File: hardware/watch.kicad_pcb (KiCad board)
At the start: 4 copper layers, 39.1 x 36.1 mm, 77 parts, among them J1 DX07S016JA1R1500, J601 SWD, Q1 DMN6140L, Q401 DMP2110UW-7, Q701 DMP2110UW-7, SW601 SW_Push, SW602 SW_Push, U12 TCPP01-M12, U201 KCSA02-105, U202 STP08DP05, U203 KCSA02-105, U204 STP08DP05, U205 KCSA02-105, U206 STP08DP05, U207 KCSA02-105, U208 STP08DP05, U301 USBLC6-2SC6, U401 LM66100, U402 MCP73831-2-OT, U403 TLV810E, U501 TPS2115A-Q1, U502 TLV70033_SOT23-5, U601 STM32L011F4Px, U701 FT230XQ, Y601 32kHz

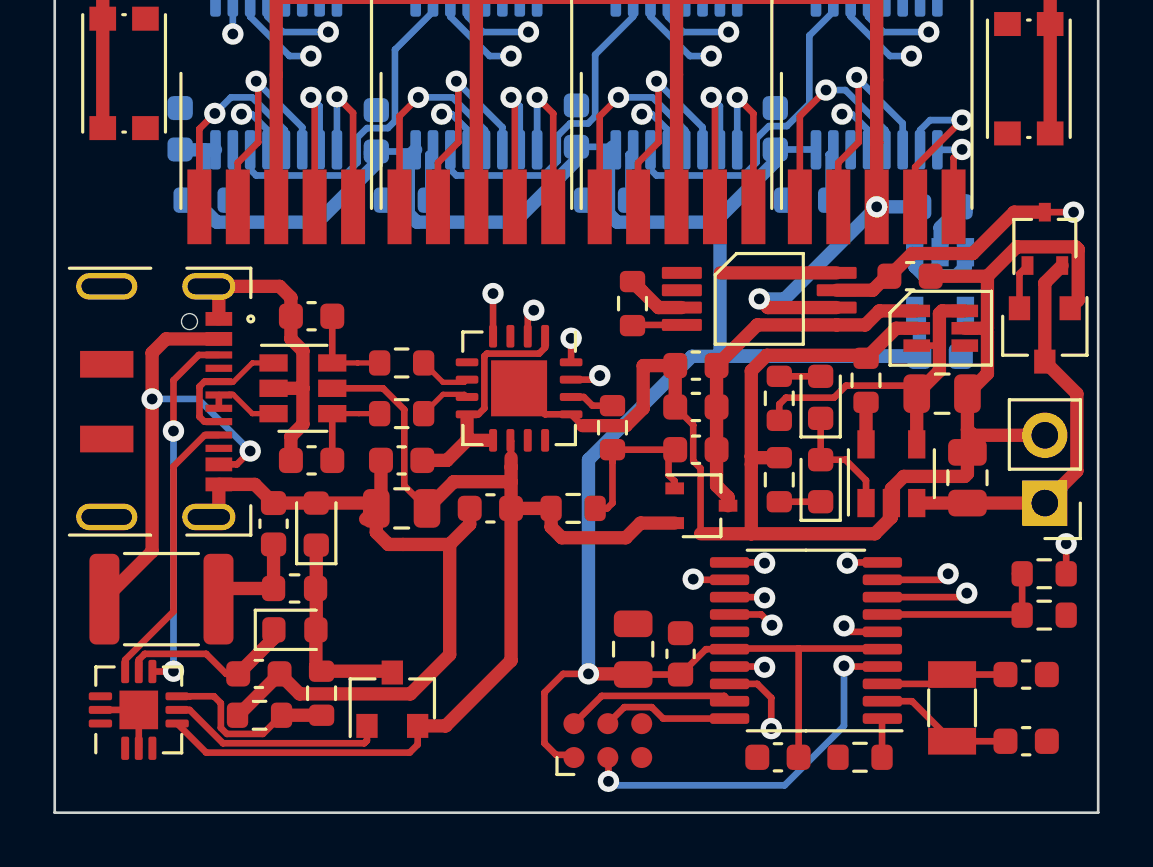
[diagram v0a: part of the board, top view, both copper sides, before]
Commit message: added some vias to gnd plane
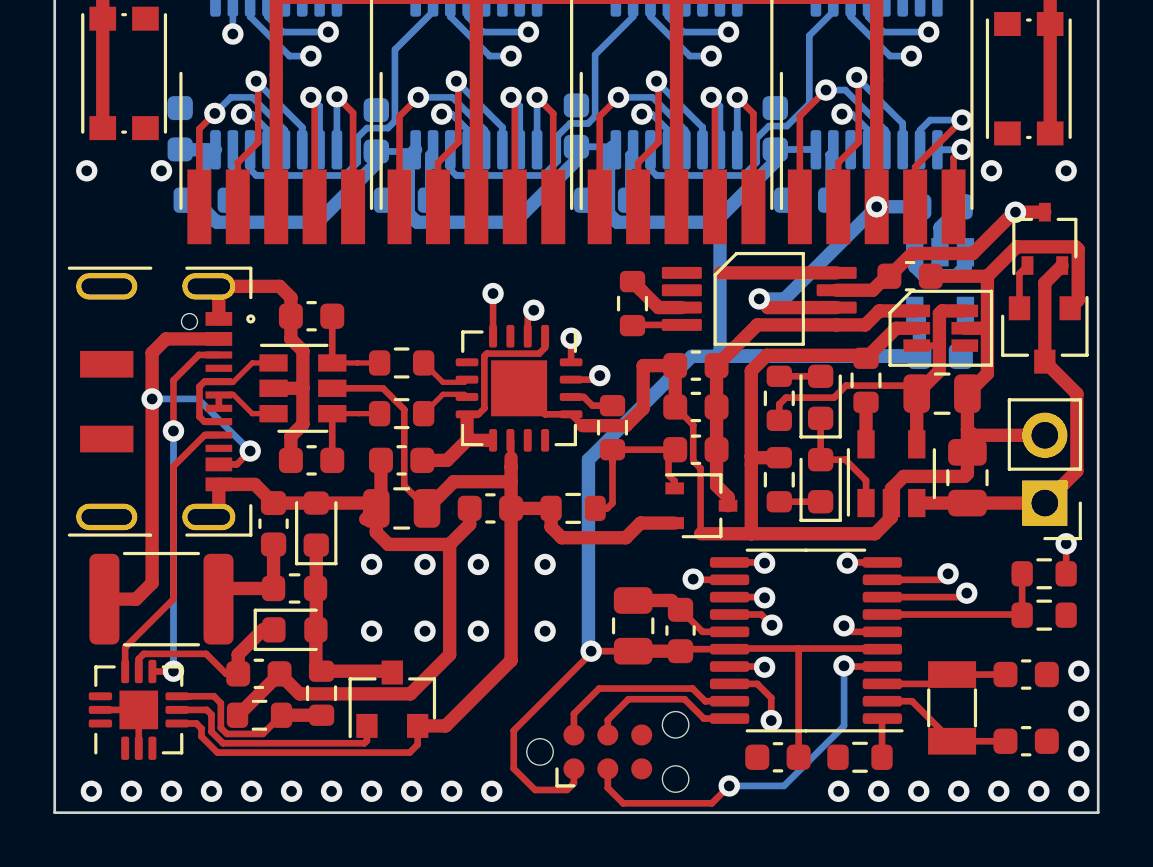
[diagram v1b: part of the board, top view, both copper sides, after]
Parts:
- moved C605 0.88 mm to (144.4, 126.2)
- moved C607 0.88 mm to (146.2, 126.4)
- moved J601 0.43 mm to (143.4, 130.9)
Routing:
- net GND: track 114.5 -> 118.6 mm, vias 0 -> 33
- net +3V3: track 95.0 -> 96.7 mm
- net /Microcontroller Circuitry/SW2: track 54.4 -> 53.5 mm
- net /Microcontroller Circuitry/SWDIO: track 6.35 -> 7.22 mm
- net /Microcontroller Circuitry/SWCLK: track 5.00 -> 5.75 mm
- net /USB Protection Circuits/VBUS: track 18.6 -> 19.2 mm

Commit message: minor improvements
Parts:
- R401, R402: value 10k -> 2k7
- R403: value R -> 3k9
- R601, R603: value R_Small -> 1k
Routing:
- net GND: track 118.6 -> 119.3 mm

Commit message: more stitching vias
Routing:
- net Net-(BT401-Pad1): track 15.0 -> 16.0 mm
- net GND: vias 33 -> 53

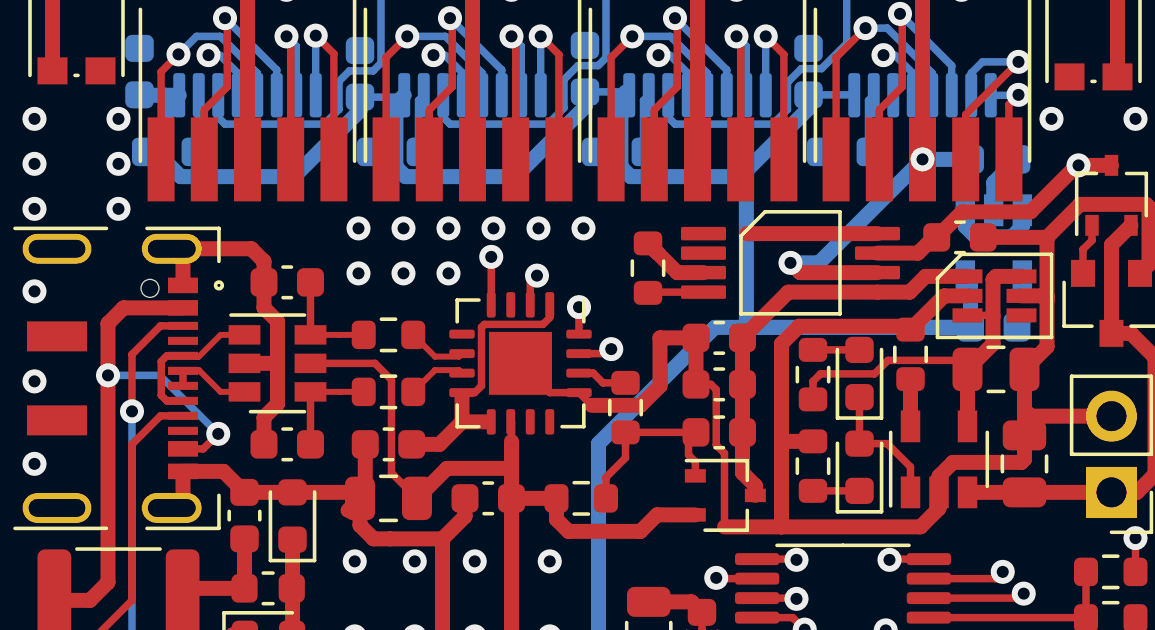
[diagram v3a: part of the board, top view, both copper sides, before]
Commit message: Fixed two hardware issues.
Issue 1: Swapped USB D+/- lines
Issue 2: Wrong schematic smybol for power switch
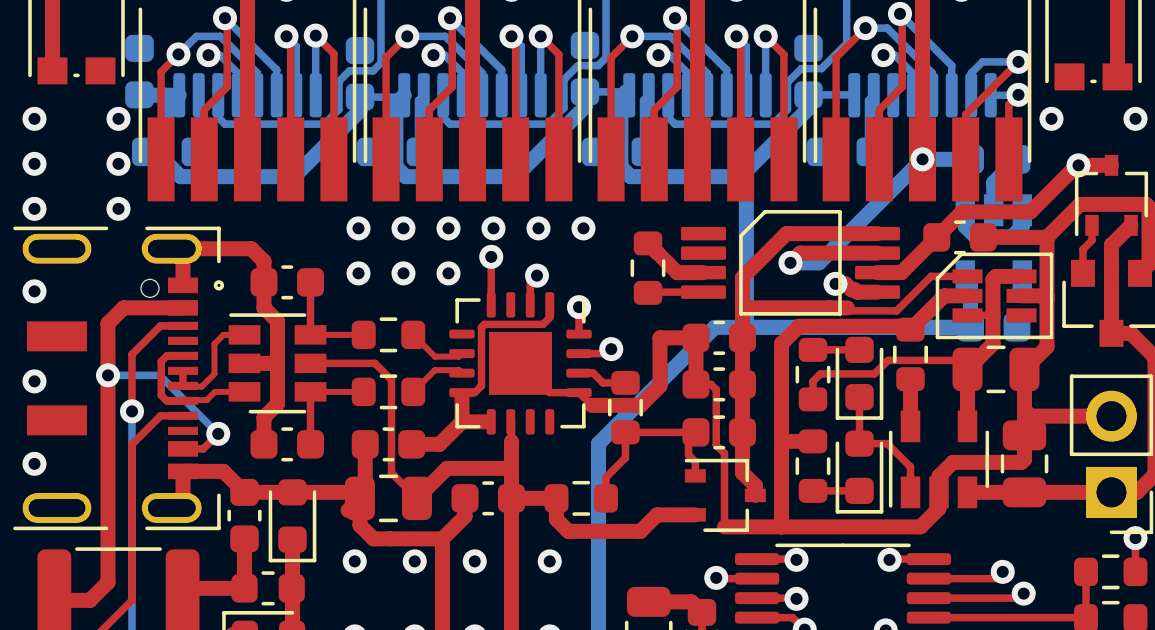
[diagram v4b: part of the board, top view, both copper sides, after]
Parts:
- BT401: value Battery_Cell -> LIPO
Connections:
- C702 pad 1: /USB/D+ -> /USB/D-
- C704 pad 1: /USB/D- -> /USB/D+
- R701 pad 1: /USB/D+ -> /USB/D-
- R701 pad 2: /USB/CHIP_D+ -> /USB/CHIP_D-
- R702 pad 1: /USB/D- -> /USB/D+
- R702 pad 2: /USB/CHIP_D- -> /USB/CHIP_D+
- U301 pad 1: /USB Protection Circuits/IN_D- -> /USB Protection Circuits/IN_D+
- U301 pad 3: /USB Protection Circuits/IN_D+ -> /USB Protection Circuits/IN_D-
- U301 pad 4: /USB/D+ -> /USB/D-
- U301 pad 6: /USB/D- -> /USB/D+
- U501 pad 5: /Power Selection Circuits/5V -> GND
- U501 pad 6: /Display/V_DISP -> /Battery Charger/VBAT
- U501 pad 7: /Battery Charger/VBAT -> /Display/V_DISP
- U501 pad 8: GND -> /Power Selection Circuits/5V
- U701 pad 6: /USB/CHIP_D- -> /USB/CHIP_D+
- U701 pad 7: /USB/CHIP_D+ -> /USB/CHIP_D-
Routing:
- net /Power Selection Circuits/5V: track 13.8 -> 21.2 mm
- net GND: track 119.3 -> 116.4 mm, vias 53 -> 54
- net /USB Protection Circuits/IN_D+: track 2.90 -> 4.30 mm

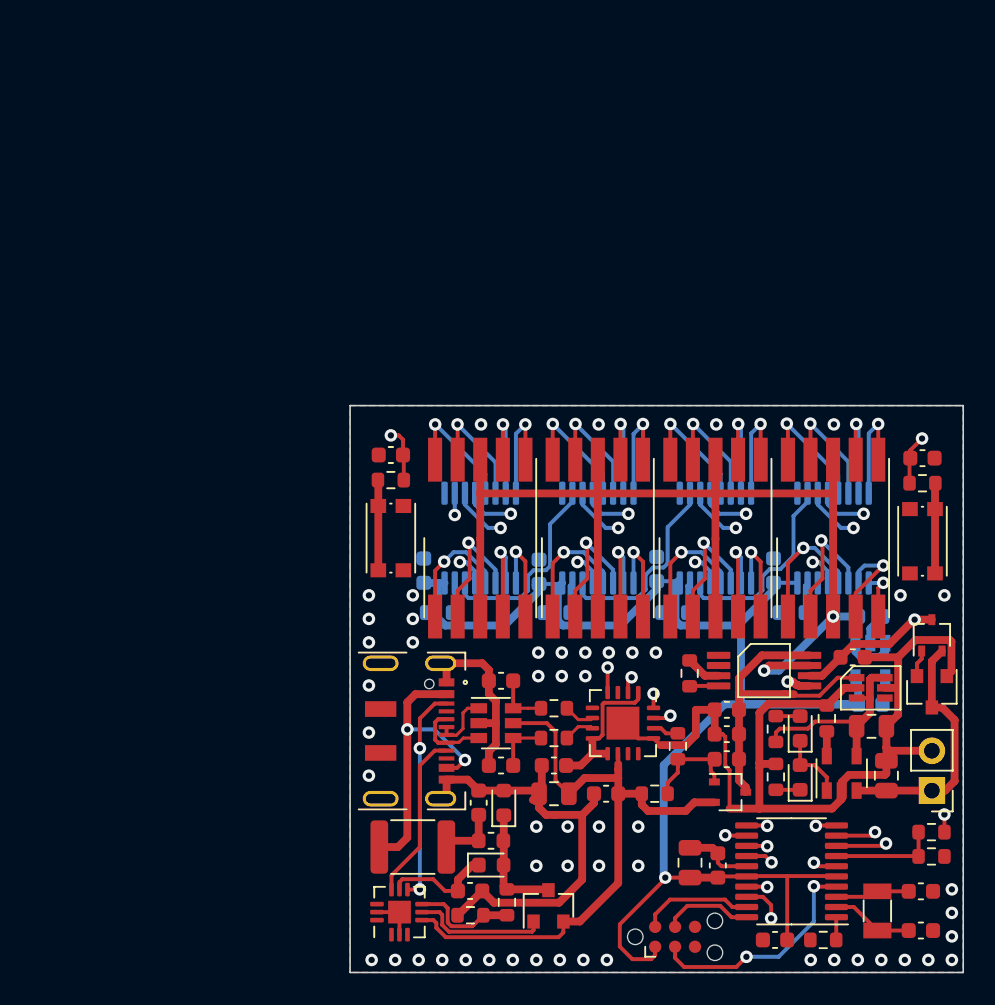
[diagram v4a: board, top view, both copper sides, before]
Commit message: New uC, ditched FTDI chip, and more!
Need to improve the schematic a little bit more.
For example, I want to be able to turn the LED Drivers off using
a MOSFET.

For the PCB Layout: I want to move as many components as possible
to the top layer, so that they are visible when in the case.
Also, I have to consider solderability of the components, the more
complex should all be on one layer for easier soldering.

Next up: Finishing the schematic, improving component placement,
and routing!
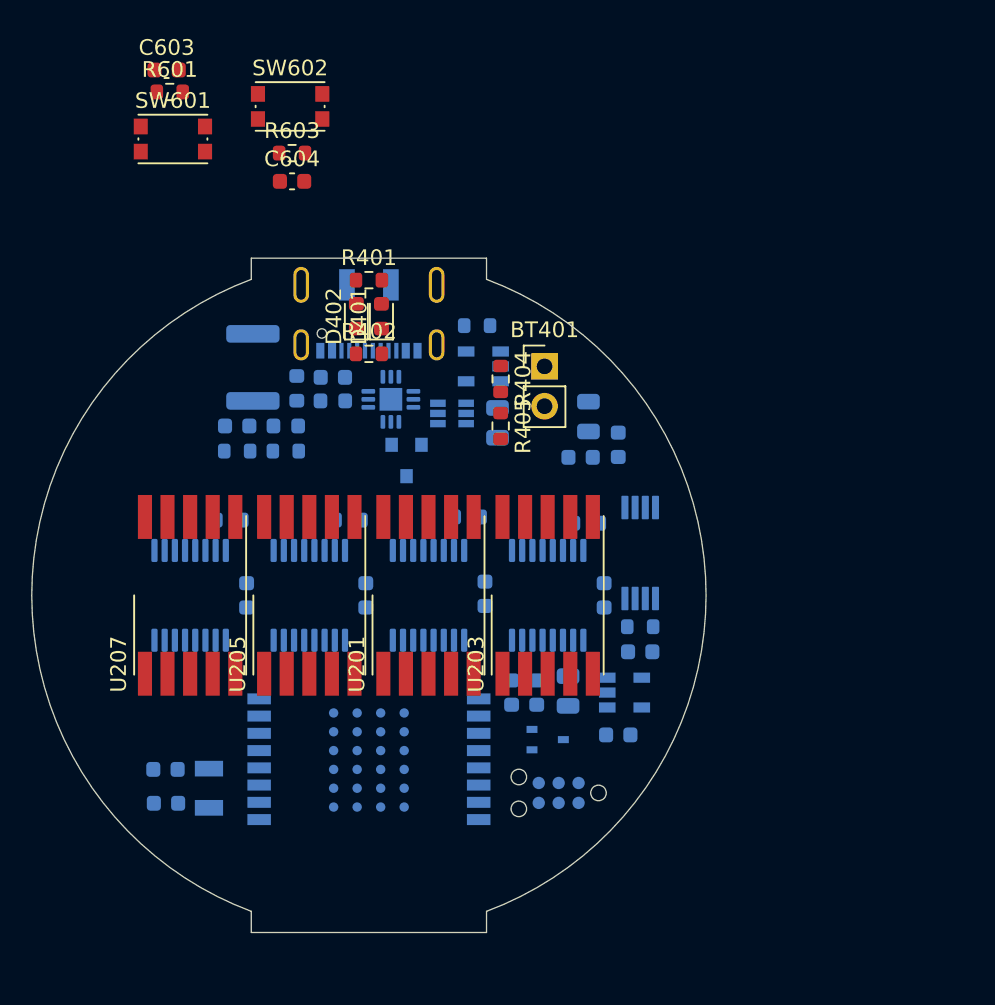
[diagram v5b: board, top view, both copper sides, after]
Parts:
- removed C701, C705, C706, C707: 100n, Capacitor_SMD:C_0603_1608Metric
- removed C702, C704: 47p, Capacitor_SMD:C_0603_1608Metric
- removed C703: 4.7u, Capacitor_SMD:C_0805_2012Metric
- removed Q701: DMP2110UW-7, Package_TO_SOT_SMD:SOT-323_SC-70
- removed R602, R703: 100k, Resistor_SMD:R_0603_1608Metric
- removed R701, R702: 27R, Resistor_SMD:R_0603_1608Metric
- removed R704: 1k, Resistor_SMD:R_0603_1608Metric
- removed U301: USBLC6-2SC6, Package_TO_SOT_SMD:SOT-23-6
- removed U403: TLV810E, Package_TO_SOT_SMD:SOT-23
- removed U601: STM32L011F4Px, Package_SO:TSSOP-20_4.4x6.5mm_P0.65mm
- removed U701: FT230XQ, Package_DFN_QFN:QFN-16-1EP_4x4mm_P0.65mm_EP2.1x2.1mm
- added U1: BT832, watch:BLEMODULE_BT832, B.Cu at (123.9, 122.7)
- C1, C301, C401, C402, C501, C502, C601, C602, C605, C606, C607, D1, D2, F301, FB301, J1, J601, Q1, Q401, R10, R11, R403, R501, U12, U401, U402, U501, Y601: moved to B.Cu
- moved SW602 48.9 mm to (118.9, 78.0), turned to 0 degrees
- moved C601 48.8 mm to (111.0, 122.4), turned to 180 degrees
- moved C602 48.8 mm to (110.9, 120.2), turned to 180 degrees
- moved R603 45.4 mm to (119.0, 81.0)
- moved C604 43.9 mm to (119.0, 82.8)
- moved Y601 43.3 mm to (113.7, 121.5)
- moved U207 41.2 mm to (112.5, 109.2)
- moved D402 40.8 mm to (123.1, 91.3)
- moved R404 39.9 mm to (132.3, 95.3), turned to 270 degrees
- moved R405 38.8 mm to (132.3, 98.3), turned to 270 degrees
- moved R401 38.6 mm to (123.9, 89.0), turned to 0 degrees
- moved D401 37.5 mm to (124.7, 91.3)
- moved R402 37.4 mm to (123.9, 93.8), turned to 0 degrees
- moved BT401 36.6 mm to (135.1, 94.5), turned to 0 degrees
- moved U402 34.6 mm to (131.2, 94.5), turned to 180 degrees
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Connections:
- net /USB Protection Circuits/IN_D+ renamed Net-(J1-PadA6)
- net /USB Protection Circuits/IN_D- renamed Net-(J1-PadA7)
- BT401 pad 1: Net-(BT401-Pad1) -> /Battery Charger/VBAT
- C402 pad 1: Net-(BT401-Pad1) -> /Battery Charger/VBAT
- Q1 pad 2: /USB Protection Circuits/5V@500mA -> /Power Selection Circuits/5V
- Q401 pad 2: Net-(BT401-Pad1) -> Net-(Q401-Pad2)
- Q401 pad 3: /Battery Charger/VBAT -> Net-(Q401-Pad3)
- U12 pad 4: /USB Protection Circuits/5V@500mA -> /Power Selection Circuits/5V
- U402 pad 3: Net-(BT401-Pad1) -> /Battery Charger/VBAT
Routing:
- net GND: track 116.4 -> 0.00 mm, vias 54 -> 0
- net +3V3: track 96.7 -> 0.00 mm, vias 1 -> 0
- net /Display/V_DISP: track 82.3 -> 0.00 mm, vias 2 -> 0
- net /Display/CLK: track 60.3 -> 0.00 mm, vias 5 -> 0
- net /Display/LE: track 58.0 -> 0.00 mm, vias 5 -> 0
- net /Microcontroller Circuitry/MOSI: track 56.3 -> 0.00 mm, vias 2 -> 0
- net /Display/OE: track 54.1 -> 0.00 mm, vias 5 -> 0
- net /Microcontroller Circuitry/SW2: track 53.8 -> 0.00 mm, vias 2 -> 0
- net /USB Protection Circuits/5V@500mA: track 46.7 -> 0.00 mm
- net /Microcontroller Circuitry/SW1: track 35.2 -> 0.00 mm, vias 2 -> 0
- net /USB/RX: track 32.5 -> 0.00 mm, vias 2 -> 0
- net /Microcontroller Circuitry/RX: track 27.8 -> 0.00 mm, vias 2 -> 0
- net /USB/CTS: track 27.6 -> 0.00 mm, vias 2 -> 0
- net /Battery Charger/VBAT: track 24.0 -> 0.00 mm, vias 2 -> 0
- net /Power Selection Circuits/5V: track 21.2 -> 0.00 mm
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- removed copper zone on B.Cu, net GND
- removed copper zone on F.Cu, net GND
- removed copper zone on In1.Cu, net GND
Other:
- board size 39.1 x 36.1 mm -> 43 x 43 mm

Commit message: Updated to KiCad v6.0
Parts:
- removed Q401: DMP2110UW-7, Package_TO_SOT_SMD:SOT-323_SC-70
- added Q2: DMP2110UW-7, Package_TO_SOT_SMD:SOT-323_SC-70, F.Cu at (140.9, 116.3)
- added R1: 1k, Resistor_SMD:R_0603_1608Metric, B.Cu at (133.6, 119.0)
- C1, C301, C401, C402, C501, C502, C503, C504, D1, D2, F301, FB301, Q1, R10, R11, R403, R501, U12, U401, U402, U501, U502: moved to F.Cu
- moved C503 9.42 mm to (133.2, 117.8), turned to 90 degrees
- moved Q1 5.04 mm to (121.4, 99.3), turned to 180 degrees
- moved C402 4.96 mm to (134.2, 94.5)
- moved U502 4.86 mm to (136.0, 117.8)
- moved C502 4.48 mm to (141.6, 103.7), turned to 90 degrees
- moved C501 4.26 mm to (140.1, 103.7), turned to 90 degrees
- moved FB301 3.67 mm to (115.0, 97.7)
- moved R404 3.44 mm to (134.3, 98.2)
- moved C301 3.00 mm to (112.5, 98.3), turned to -90 degrees
- moved U501 2.70 mm to (141.1, 109.2), turned to 0 degrees
- moved R501 2.70 mm to (141.1, 113.8), turned to 180 degrees
- moved R405 2.49 mm to (133.5, 100.5), turned to 180 degrees
- moved BT401 2.25 mm to (137.0, 95.8)
- moved R10 1.86 mm to (117.5, 98.5), turned to -90 degrees
- moved C504 1.17 mm to (138.7, 117.7), turned to -90 degrees
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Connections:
- C201 pad 1: +3V3 -> /Display/POWER_IN
- C202 pad 1: +3V3 -> /Display/POWER_IN
- C203 pad 1: +3V3 -> /Display/POWER_IN
- C204 pad 1: +3V3 -> /Display/POWER_IN
- C503 pad 1: /Display/V_DISP -> Net-(C503-Pad1)
- C504 pad 1: +3V3 -> /Power Selection Circuits/VuC
- C605 pad 1: +3V3 -> /Microcontroller Circuitry/VIN
- C606 pad 1: +3V3 -> /Microcontroller Circuitry/VIN
- C607 pad 1: +3V3 -> /Microcontroller Circuitry/VIN
- J1 pad B6: Net-(J1-PadA6) -> Net-(J1-PadB6)
- J1 pad B7: Net-(J1-PadA7) -> Net-(J1-PadB7)
- J601 pad 1: +3V3 -> /Microcontroller Circuitry/VIN
- U1 pad 12: /Microcontroller Circuitry/LED-POWER -> /Power Selection Circuits/LED_CTRL
- U1 pad 9: +3V3 -> /Microcontroller Circuitry/VIN
- U202 pad 16: +3V3 -> /Display/POWER_IN
- U204 pad 16: +3V3 -> /Display/POWER_IN
- U206 pad 16: +3V3 -> /Display/POWER_IN
- U208 pad 16: +3V3 -> /Display/POWER_IN
- U501 pad 7: /Display/V_DISP -> Net-(C503-Pad1)
- U502 pad 1: /Display/V_DISP -> Net-(C503-Pad1)
- U502 pad 3: /Display/V_DISP -> Net-(C503-Pad1)
- U502 pad 5: +3V3 -> /Power Selection Circuits/VuC
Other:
- net class Default removed
